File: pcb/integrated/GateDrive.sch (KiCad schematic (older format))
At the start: 14 parts, among them U11001 UCC5350SB, U11002 R15P21503D

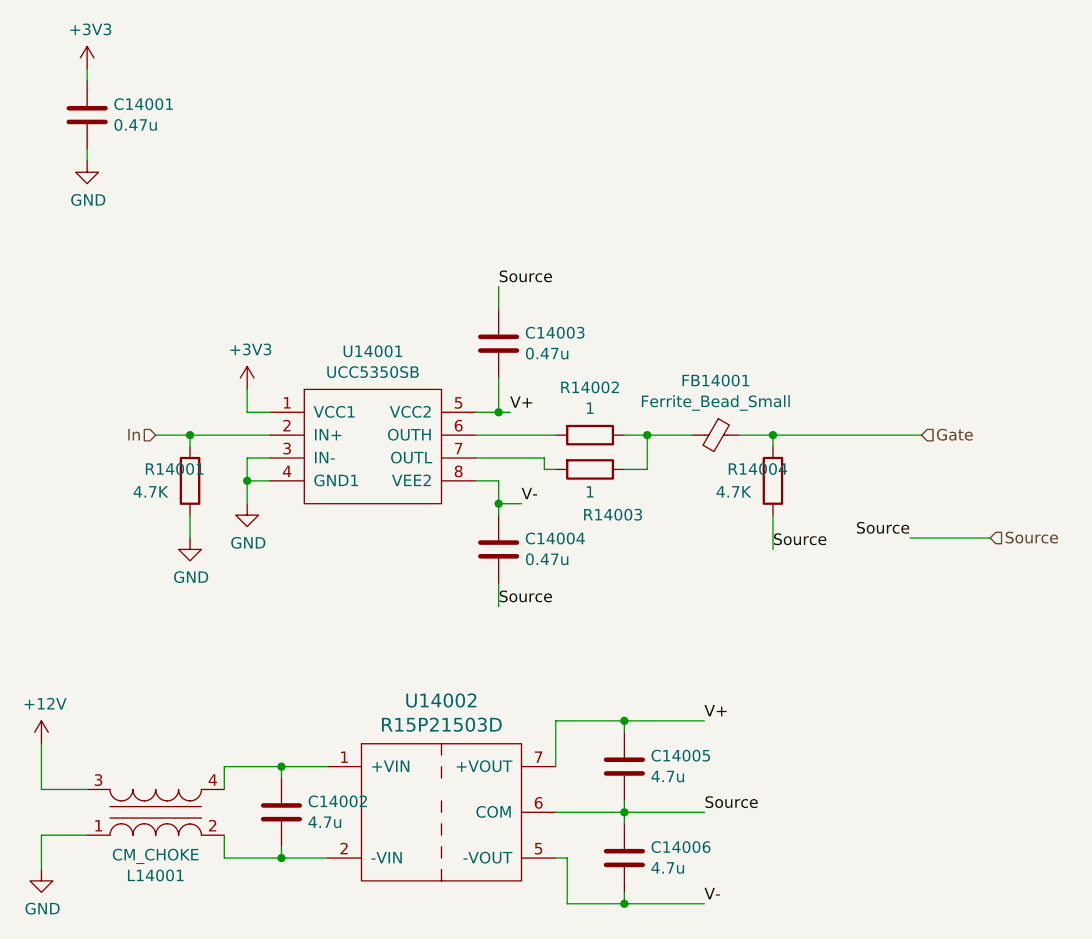
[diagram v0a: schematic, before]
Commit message: redid power planes
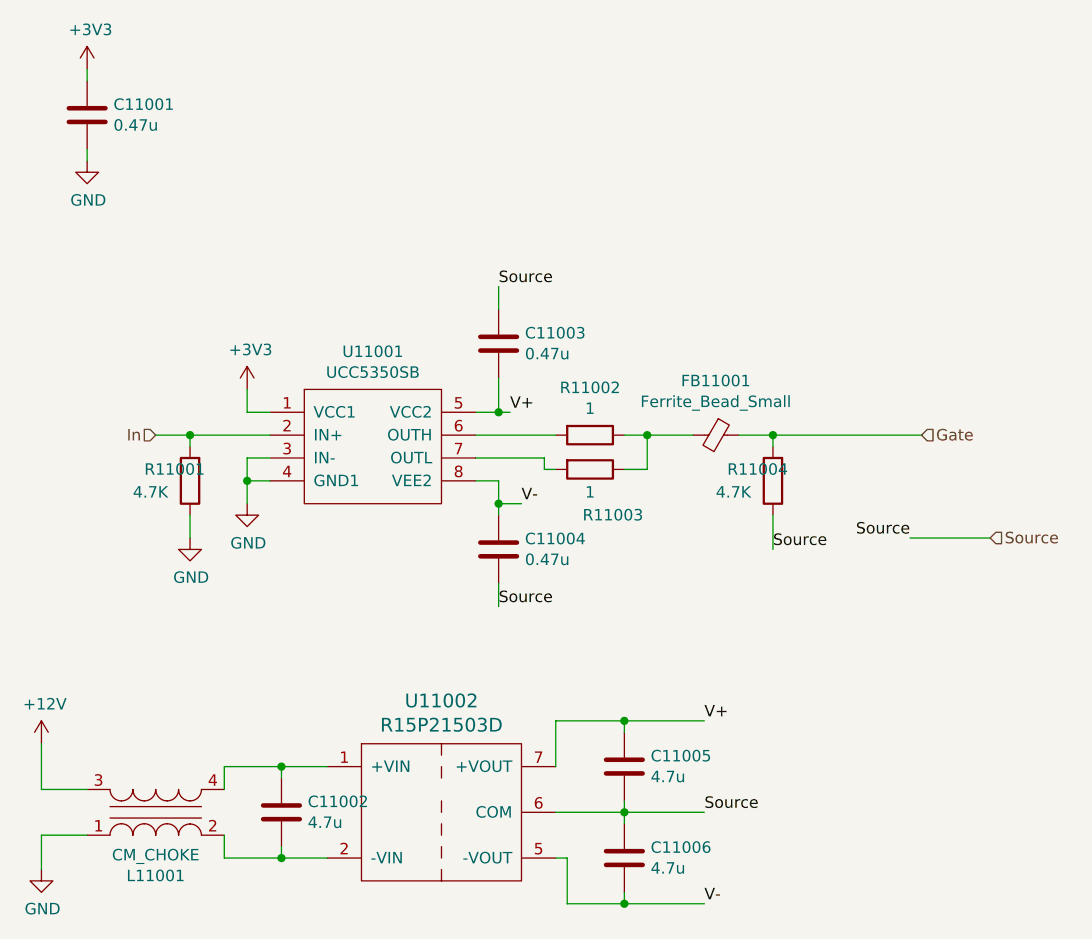
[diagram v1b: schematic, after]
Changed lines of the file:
@@
 AR Path="/5D68A538/5D640674/5DD374B5" Ref="U13002"  Part="1"
 AR Path="/5D68A538/5D640682/5DD374B5" Ref="U14002"  Part="1"
-F 0 "U14002" H 3450 5237 60  0000 C CNN
+F 0 "U11002" H 3450 5237 60  0000 C CNN
 F 1 "R15P21503D" H 3450 5131 60  0000 C CNN
 F 2 "wbraun_smd:SIP7-5" H 3450 4850 60  0001 C CNN
@@
 AR Path="/5D68A538/5D640674/5DD374B6" Ref="U13001"  Part="1"
 AR Path="/5D68A538/5D640682/5DD374B6" Ref="U14001"  Part="1"
-F 0 "U14001" H 3150 3565 50  0000 C CNN
+F 0 "U11001" H 3150 3565 50  0000 C CNN
 F 1 "UCC5350SB" H 3150 3474 50  0000 C CNN
 F 2 "Package_SO:SOIC-8_3.9x4.9mm_P1.27mm" H 2800 3200 50  0001 C CNN
@@
 AR Path="/5D68A538/5D640674/5DD374B7" Ref="C13002"  Part="1"
 AR Path="/5D68A538/5D640682/5DD374B7" Ref="C14002"  Part="1"
-F 0 "C14002" H 2865 4796 50  0000 L CNN
+F 0 "C11002" H 2865 4796 50  0000 L CNN
 F 1 "4.7u" H 2865 4705 50  0000 L CNN
 F 2 "Capacitor_SMD:C_0805_2012Metric" H 2788 4600 50  0001 C CNN
@@
 AR Path="/5D68A538/5D640674/5D630902" Ref="C13005"  Part="1"
 AR Path="/5D68A538/5D640682/5D630902" Ref="C14005"  Part="1"
-F 0 "C14005" H 4365 4596 50  0000 L CNN
+F 0 "C11005" H 4365 4596 50  0000 L CNN
 F 1 "4.7u" H 4365 4505 50  0000 L CNN
 F 2 "Capacitor_SMD:C_0805_2012Metric" H 4288 4400 50  0001 C CNN
@@
 AR Path="/5D68A538/5D640674/5D630909" Ref="C13006"  Part="1"
 AR Path="/5D68A538/5D640682/5D630909" Ref="C14006"  Part="1"
-F 0 "C14006" H 4365 4996 50  0000 L CNN
+F 0 "C11006" H 4365 4996 50  0000 L CNN
 F 1 "4.7u" H 4365 4905 50  0000 L CNN
 F 2 "Capacitor_SMD:C_0805_2012Metric" H 4288 4800 50  0001 C CNN
@@
 AR Path="/5D68A538/5D640674/5D630910" Ref="C13003"  Part="1"
 AR Path="/5D68A538/5D640682/5D630910" Ref="C14003"  Part="1"
-F 0 "C14003" H 3815 2746 50  0000 L CNN
+F 0 "C11003" H 3815 2746 50  0000 L CNN
 F 1 "0.47u" H 3815 2655 50  0000 L CNN
 F 2 "Capacitor_SMD:C_0603_1608Metric" H 3738 2550 50  0001 C CNN
@@
 AR Path="/5D68A538/5D640674/5DD374BB" Ref="C13004"  Part="1"
 AR Path="/5D68A538/5D640682/5DD374BB" Ref="C14004"  Part="1"
-F 0 "C14004" H 3815 3646 50  0000 L CNN
+F 0 "C11004" H 3815 3646 50  0000 L CNN
 F 1 "0.47u" H 3815 3555 50  0000 L CNN
 F 2 "Capacitor_SMD:C_0603_1608Metric" H 3738 3450 50  0001 C CNN
@@
 AR Path="/5D68A538/5D640674/5D63091E" Ref="R13002"  Part="1"
 AR Path="/5D68A538/5D640682/5D63091E" Ref="R14002"  Part="1"
-F 0 "R14002" V 3893 3100 50  0000 C CNN
+F 0 "R11002" V 3893 3100 50  0000 C CNN
 F 1 "1" V 3984 3100 50  0000 C CNN
 F 2 "Resistor_SMD:R_0805_2012Metric" V 4030 3100 50  0001 C CNN
@@
 AR Path="/5D68A538/5D640674/5D630925" Ref="R13003"  Part="1"
 AR Path="/5D68A538/5D640682/5D630925" Ref="R14003"  Part="1"
-F 0 "R14003" V 4300 3350 50  0000 C CNN
+F 0 "R11003" V 4300 3350 50  0000 C CNN
 F 1 "1" V 4200 3250 50  0000 C CNN
 F 2 "Resistor_SMD:R_0805_2012Metric" V 4030 3250 50  0001 C CNN
@@
 AR Path="/5D68A538/5D640674/5D63094B" Ref="R13001"  Part="1"
 AR Path="/5D68A538/5D640682/5D63094B" Ref="R14001"  Part="1"
-F 0 "R14001" H 2550 3250 50  0000 R CNN
+F 0 "R11001" H 2550 3250 50  0000 R CNN
 F 1 "4.7K" H 2600 3350 50  0000 R CNN
 F 2 "Resistor_SMD:R_0603_1608Metric" V 2280 3300 50  0001 C CNN
@@
 AR Path="/5D68A538/5D640674/5D630960" Ref="C13001"  Part="1"
 AR Path="/5D68A538/5D640682/5D630960" Ref="C14001"  Part="1"
-F 0 "C14001" H 2015 1746 50  0000 L CNN
+F 0 "C11001" H 2015 1746 50  0000 L CNN
 F 1 "0.47u" H 2015 1655 50  0000 L CNN
 F 2 "Capacitor_SMD:C_0603_1608Metric" H 1938 1550 50  0001 C CNN
@@
 AR Path="/5D68A538/5D640674/5D63A672" Ref="FB13001"  Part="1"
 AR Path="/5D68A538/5D640682/5D63A672" Ref="FB14001"  Part="1"
-F 0 "FB14001" V 4413 3100 50  0000 C CNN
+F 0 "FB11001" V 4413 3100 50  0000 C CNN
 F 1 "Ferrite_Bead_Small" V 4504 3100 50  0000 C CNN
 F 2 "Inductor_SMD:L_0805_2012Metric" V 4580 3100 50  0001 C CNN
@@
 AR Path="/5D68A538/5D640674/5DD374C9" Ref="R13004"  Part="1"
 AR Path="/5D68A538/5D640682/5DD374C9" Ref="R14004"  Part="1"
-F 0 "R14004" H 5100 3250 50  0000 R CNN
+F 0 "R11004" H 5100 3250 50  0000 R CNN
 F 1 "4.7K" H 5150 3350 50  0000 R CNN
 F 2 "Resistor_SMD:R_0603_1608Metric" V 4830 3300 50  0001 C CNN
@@
 AR Path="/5D68A538/5D640674/5D63092C" Ref="L13001"  Part="1"
 AR Path="/5D68A538/5D640682/5D63092C" Ref="L14001"  Part="1"
-F 0 "L14001" H 2200 5028 50  0000 C CNN
+F 0 "L11001" H 2200 5028 50  0000 C CNN
 F 1 "CM_CHOKE" H 2200 4937 50  0000 C CNN
 F 2 "wbraun_smd:SRF2012" V 2200 4750 50  0001 C CNN

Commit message: PCB routing finihsed, ready for design review
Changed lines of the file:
@@
 AR Path="/5D68A538/5D640674/5DD374B5" Ref="U13002"  Part="1"
 AR Path="/5D68A538/5D640682/5DD374B5" Ref="U14002"  Part="1"
-F 0 "U11002" H 3450 5237 60  0000 C CNN
+F 0 "U14002" H 3450 5237 60  0000 C CNN
 F 1 "R15P21503D" H 3450 5131 60  0000 C CNN
 F 2 "wbraun_smd:SIP7-5" H 3450 4850 60  0001 C CNN
@@
 AR Path="/5D68A538/5D640674/5DD374B6" Ref="U13001"  Part="1"
 AR Path="/5D68A538/5D640682/5DD374B6" Ref="U14001"  Part="1"
-F 0 "U11001" H 3150 3565 50  0000 C CNN
+F 0 "U14001" H 3150 3565 50  0000 C CNN
 F 1 "UCC5350SB" H 3150 3474 50  0000 C CNN
 F 2 "Package_SO:SOIC-8_3.9x4.9mm_P1.27mm" H 2800 3200 50  0001 C CNN
@@
 AR Path="/5D68A538/5D640674/5DD374B7" Ref="C13002"  Part="1"
 AR Path="/5D68A538/5D640682/5DD374B7" Ref="C14002"  Part="1"
-F 0 "C11002" H 2865 4796 50  0000 L CNN
+F 0 "C14002" H 2865 4796 50  0000 L CNN
 F 1 "4.7u" H 2865 4705 50  0000 L CNN
 F 2 "Capacitor_SMD:C_0805_2012Metric" H 2788 4600 50  0001 C CNN
@@
 AR Path="/5D68A538/5D640674/5D630902" Ref="C13005"  Part="1"
 AR Path="/5D68A538/5D640682/5D630902" Ref="C14005"  Part="1"
-F 0 "C11005" H 4365 4596 50  0000 L CNN
+F 0 "C14005" H 4365 4596 50  0000 L CNN
 F 1 "4.7u" H 4365 4505 50  0000 L CNN
 F 2 "Capacitor_SMD:C_0805_2012Metric" H 4288 4400 50  0001 C CNN
@@
 AR Path="/5D68A538/5D640674/5D630909" Ref="C13006"  Part="1"
 AR Path="/5D68A538/5D640682/5D630909" Ref="C14006"  Part="1"
-F 0 "C11006" H 4365 4996 50  0000 L CNN
+F 0 "C14006" H 4365 4996 50  0000 L CNN
 F 1 "4.7u" H 4365 4905 50  0000 L CNN
 F 2 "Capacitor_SMD:C_0805_2012Metric" H 4288 4800 50  0001 C CNN
@@
 AR Path="/5D68A538/5D640674/5D630910" Ref="C13003"  Part="1"
 AR Path="/5D68A538/5D640682/5D630910" Ref="C14003"  Part="1"
-F 0 "C11003" H 3815 2746 50  0000 L CNN
+F 0 "C14003" H 3815 2746 50  0000 L CNN
 F 1 "0.47u" H 3815 2655 50  0000 L CNN
 F 2 "Capacitor_SMD:C_0603_1608Metric" H 3738 2550 50  0001 C CNN
@@
 AR Path="/5D68A538/5D640674/5DD374BB" Ref="C13004"  Part="1"
 AR Path="/5D68A538/5D640682/5DD374BB" Ref="C14004"  Part="1"
-F 0 "C11004" H 3815 3646 50  0000 L CNN
+F 0 "C14004" H 3815 3646 50  0000 L CNN
 F 1 "0.47u" H 3815 3555 50  0000 L CNN
 F 2 "Capacitor_SMD:C_0603_1608Metric" H 3738 3450 50  0001 C CNN
@@
 AR Path="/5D68A538/5D640674/5D63091E" Ref="R13002"  Part="1"
 AR Path="/5D68A538/5D640682/5D63091E" Ref="R14002"  Part="1"
-F 0 "R11002" V 3893 3100 50  0000 C CNN
+F 0 "R14002" V 3893 3100 50  0000 C CNN
 F 1 "1" V 3984 3100 50  0000 C CNN
 F 2 "Resistor_SMD:R_0805_2012Metric" V 4030 3100 50  0001 C CNN
@@
 AR Path="/5D68A538/5D640674/5D630925" Ref="R13003"  Part="1"
 AR Path="/5D68A538/5D640682/5D630925" Ref="R14003"  Part="1"
-F 0 "R11003" V 4300 3350 50  0000 C CNN
+F 0 "R14003" V 4300 3350 50  0000 C CNN
 F 1 "1" V 4200 3250 50  0000 C CNN
 F 2 "Resistor_SMD:R_0805_2012Metric" V 4030 3250 50  0001 C CNN
@@
 AR Path="/5D68A538/5D640674/5D63094B" Ref="R13001"  Part="1"
 AR Path="/5D68A538/5D640682/5D63094B" Ref="R14001"  Part="1"
-F 0 "R11001" H 2550 3250 50  0000 R CNN
+F 0 "R14001" H 2550 3250 50  0000 R CNN
 F 1 "4.7K" H 2600 3350 50  0000 R CNN
 F 2 "Resistor_SMD:R_0603_1608Metric" V 2280 3300 50  0001 C CNN
@@
 AR Path="/5D68A538/5D640674/5D630960" Ref="C13001"  Part="1"
 AR Path="/5D68A538/5D640682/5D630960" Ref="C14001"  Part="1"
-F 0 "C11001" H 2015 1746 50  0000 L CNN
+F 0 "C14001" H 2015 1746 50  0000 L CNN
 F 1 "0.47u" H 2015 1655 50  0000 L CNN
 F 2 "Capacitor_SMD:C_0603_1608Metric" H 1938 1550 50  0001 C CNN
@@
 AR Path="/5D68A538/5D640674/5D63A672" Ref="FB13001"  Part="1"
 AR Path="/5D68A538/5D640682/5D63A672" Ref="FB14001"  Part="1"
-F 0 "FB11001" V 4413 3100 50  0000 C CNN
+F 0 "FB14001" V 4413 3100 50  0000 C CNN
 F 1 "Ferrite_Bead_Small" V 4504 3100 50  0000 C CNN
 F 2 "Inductor_SMD:L_0805_2012Metric" V 4580 3100 50  0001 C CNN
@@
 AR Path="/5D68A538/5D640674/5DD374C9" Ref="R13004"  Part="1"
 AR Path="/5D68A538/5D640682/5DD374C9" Ref="R14004"  Part="1"
-F 0 "R11004" H 5100 3250 50  0000 R CNN
+F 0 "R14004" H 5100 3250 50  0000 R CNN
 F 1 "4.7K" H 5150 3350 50  0000 R CNN
 F 2 "Resistor_SMD:R_0603_1608Metric" V 4830 3300 50  0001 C CNN
@@
 AR Path="/5D68A538/5D640674/5D63092C" Ref="L13001"  Part="1"
 AR Path="/5D68A538/5D640682/5D63092C" Ref="L14001"  Part="1"
-F 0 "L11001" H 2200 5028 50  0000 C CNN
+F 0 "L14001" H 2200 5028 50  0000 C CNN
 F 1 "CM_CHOKE" H 2200 4937 50  0000 C CNN
 F 2 "wbraun_smd:SRF2012" V 2200 4750 50  0001 C CNN
